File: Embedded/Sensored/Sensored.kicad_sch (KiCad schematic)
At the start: 14 parts, among them J2 MicroSD, U1 ICM-20948, U3 BME280

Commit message: Added Castellated Pins & Removed Micro SD Card
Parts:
- removed C10: 22uF, Capacitor_SMD:C_0603_1608Metric_Pad1.08x0.95mm_HandSolder, symbol Device:C
- removed C12: 0.1uF, Capacitor_SMD:C_0402_1005Metric, symbol Device:C
- removed J2: MicroSD, MicroSD_473092651:CONN12_47309-2651_MOL, symbol MicroSD_473092651:473092651
- added J1: Casselation, Simple_Connector:1mm_4P, symbol Connector:Conn_01x04_Socket
- added R1, R2: 10K, Resistor_SMD:R_0402_1005Metric, symbol Device:R
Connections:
- net Vin is gone; now on net +3V3: C9.1, U4.3 (EN), U4.4 (IN)
- net +3V3: now also J1.1 (Pin_1), R1.1, R2.1
- net GND: now also J1.4 (Pin_4)
- net SCL: now also J1.3 (Pin_3), R1.2
- net SDA: now also J1.2 (Pin_2), R2.2
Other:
- moved on the sheet: C1, C3, C4, C6, C8, U1, U3

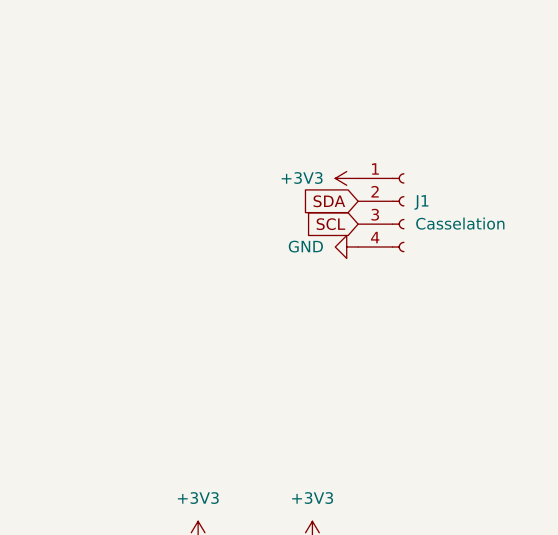
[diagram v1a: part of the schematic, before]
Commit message: Added Stabiliser GND Pins & Finished Routing
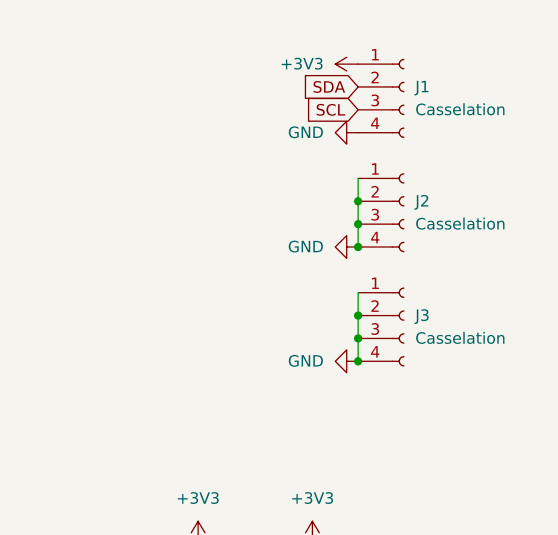
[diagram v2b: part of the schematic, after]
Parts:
- added J2, J3: Casselation, Simple_Connector:1mm_4P, symbol Connector:Conn_01x04_Socket
- C11, C9: footprint Resistor_SMD:R_0603_1608Metric -> Resistor_SMD:R_0402_1005Metric
- C13: footprint Capacitor_SMD:C_0603_1608Metric -> Capacitor_SMD:C_0402_1005Metric
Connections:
- net GND: now also J2.1 (Pin_1), J2.2 (Pin_2), J2.3 (Pin_3), J2.4 (Pin_4), J3.1 (Pin_1), J3.2 (Pin_2), J3.3 (Pin_3), J3.4 (Pin_4)
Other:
- moved on the sheet: J1

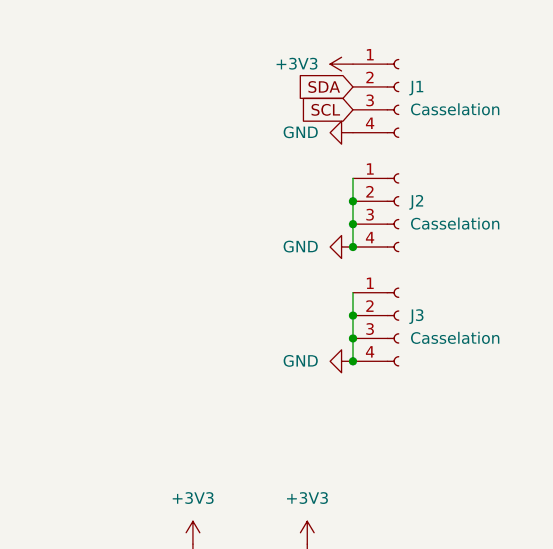
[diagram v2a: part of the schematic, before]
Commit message: Replaced Side GND Pins with GND EPad
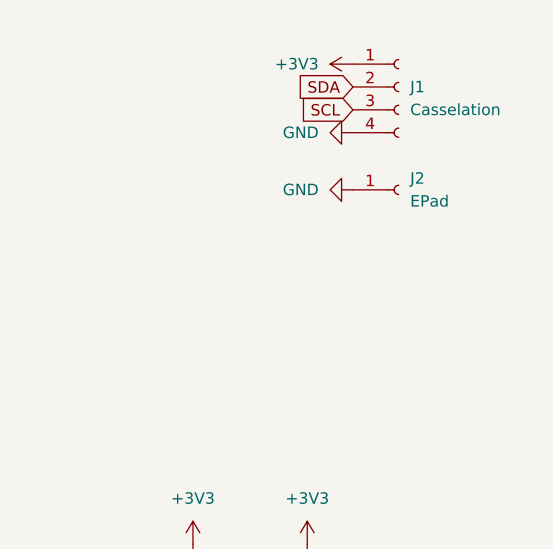
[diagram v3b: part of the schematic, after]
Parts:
- removed J2, J3: Casselation, Simple_Connector:1mm_4P, symbol Connector:Conn_01x04_Socket
- added J2: EPad, Simple_Connector:1mm 3x3 Pad, symbol Connector:Conn_01x01_Socket
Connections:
- net GND: now also J2.1 (Pin_1)
